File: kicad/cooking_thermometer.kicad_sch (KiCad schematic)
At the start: 41 parts, among them J1 FTDI, J2 STLINK, J3 3V3_Power, J4 Battery, J5 7SEG_CONN, J6 OLED_CONN, J7 USB_B_Micro, J8 THERMO_CONN, Q1 BC547, SW1 BOOT0_SW, SW2 NRST_SW, SW3 UI_A_SW, SW4 UI_B_SW, SW5 UI_C_SW, U1 STM32F070F6Px, U2 MCP1700x-330xxTO, U3 MCP73831-2-OT

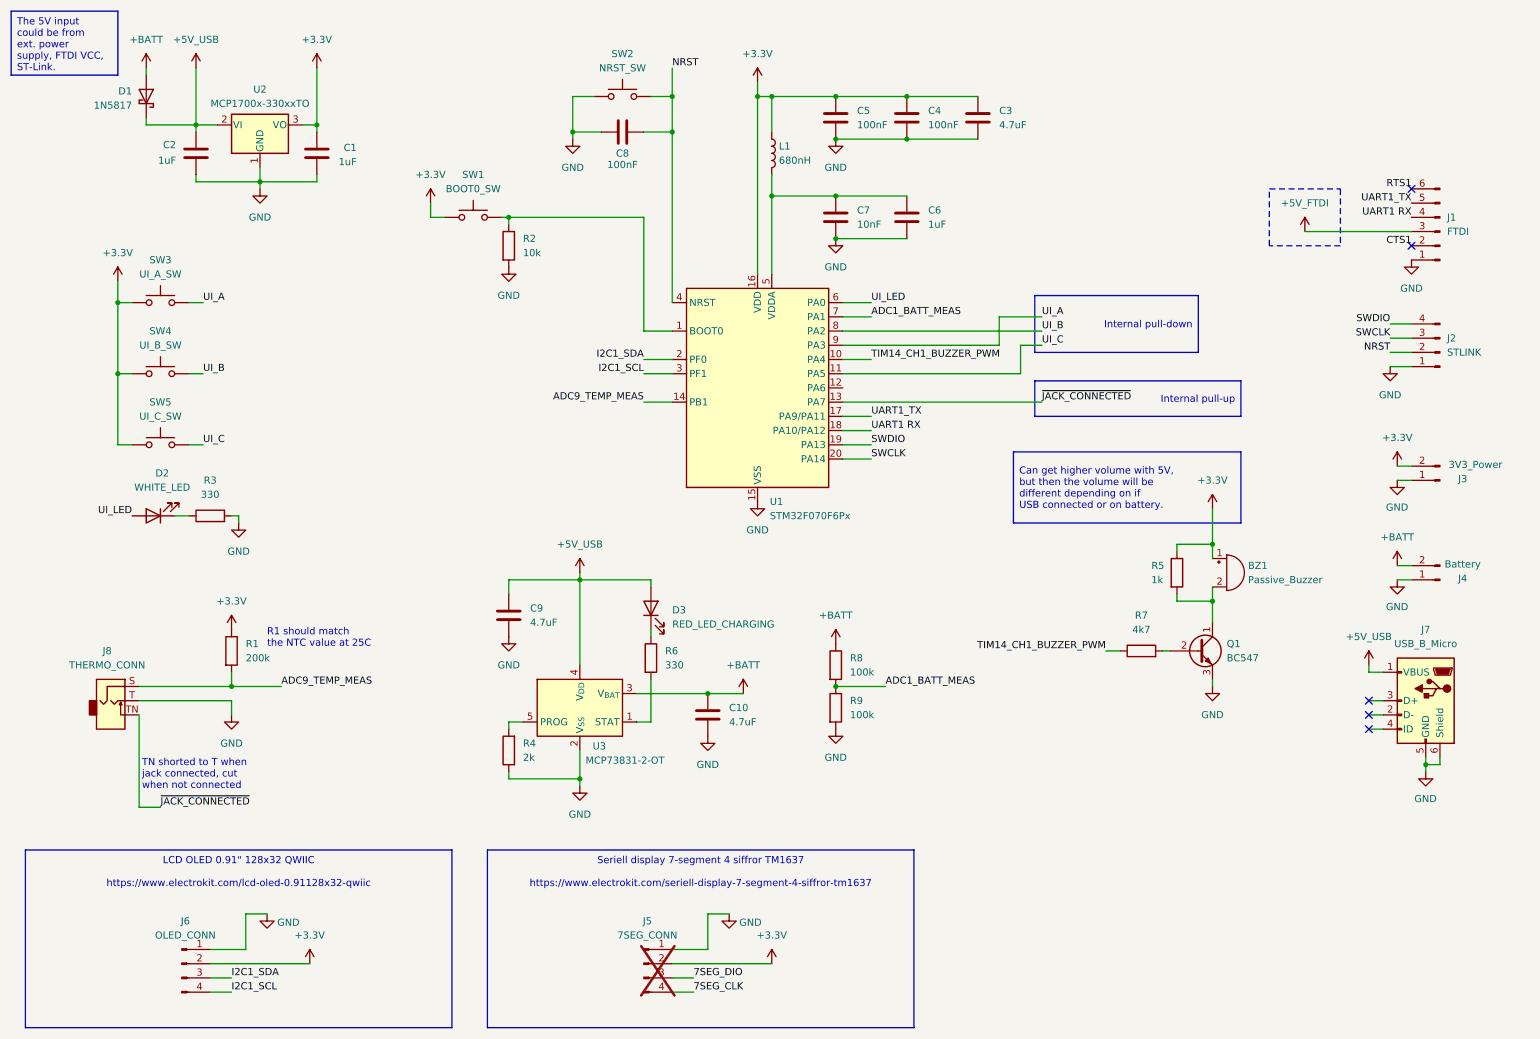
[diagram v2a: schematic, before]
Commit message: Change schematic/layout to stm32g0b0ke (LQFP32)
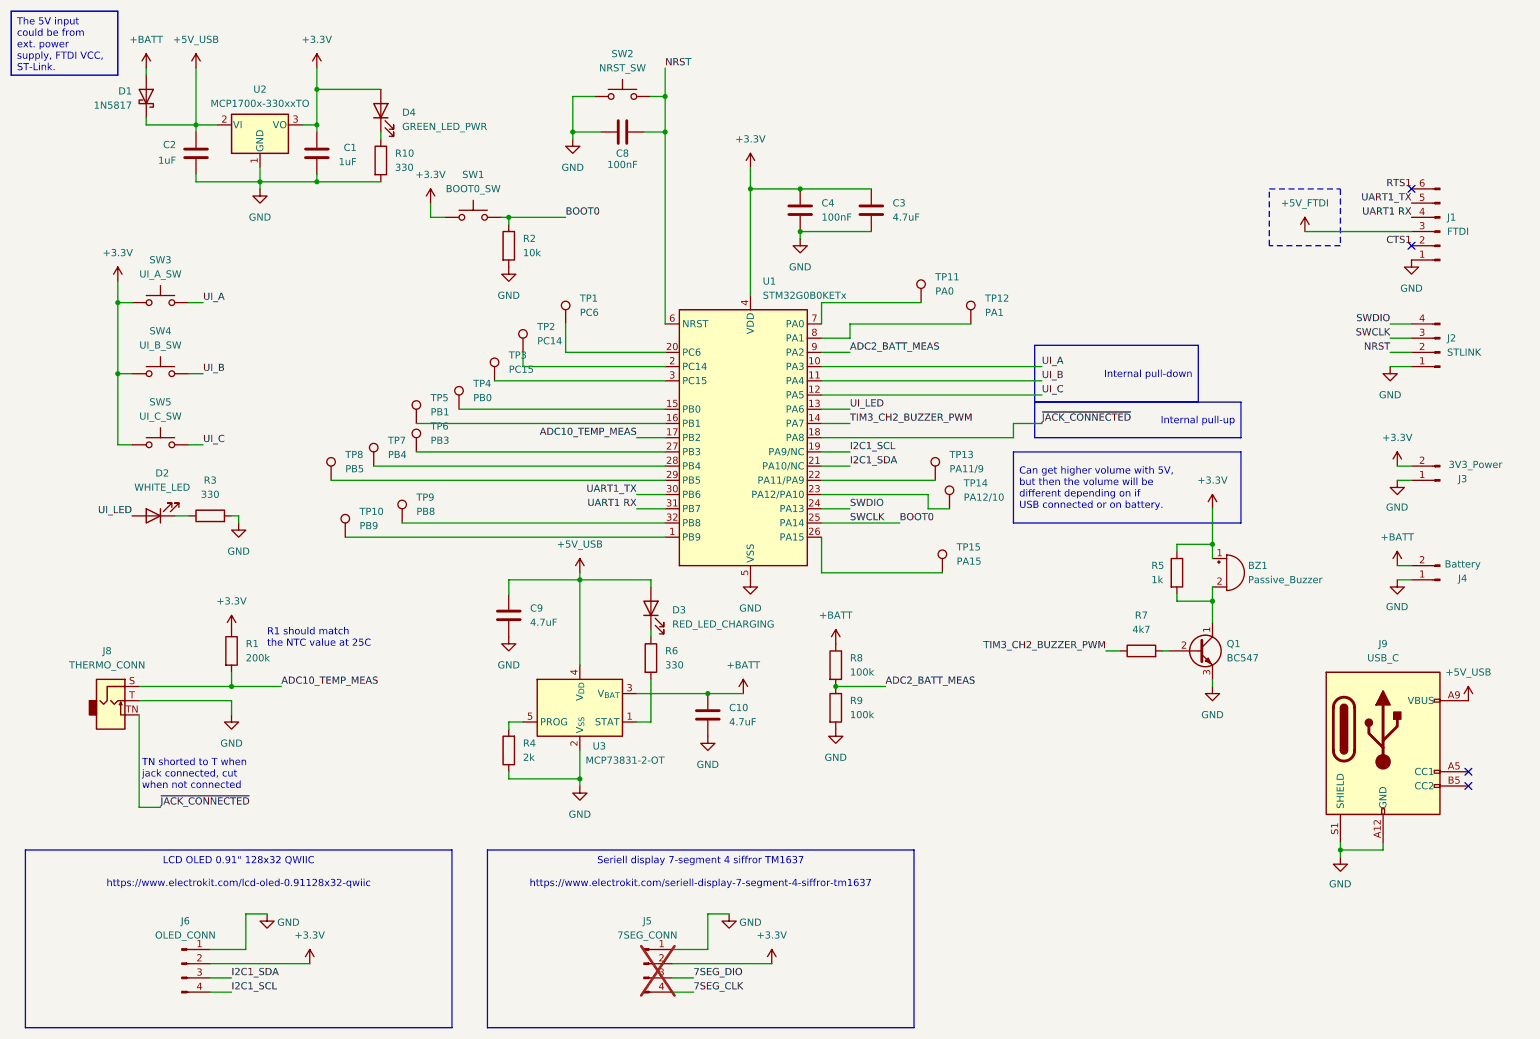
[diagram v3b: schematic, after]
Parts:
- removed C5: 100nF, Capacitor_THT:C_Disc_D3.0mm_W1.6mm_P2.50mm, symbol Device:C
- removed C6: 1uF, Capacitor_THT:C_Disc_D3.0mm_W1.6mm_P2.50mm, symbol Device:C
- removed C7: 10nF, Capacitor_THT:C_Disc_D3.0mm_W1.6mm_P2.50mm, symbol Device:C
- removed J7: USB_B_Micro, MyOwnFootprintLibrary:uUSB-B_2.54mm_connector, symbol Connector:USB_B_Micro
- removed L1: 680nH, Inductor_THT:L_Axial_L12.0mm_D5.0mm_P15.24mm_Horizontal_Fastron_MISC, symbol Device:L
- removed U1: STM32F070F6Px, MyOwnFootprintLibrary:STM32F070_DIP20, symbol MCU_ST_STM32F0:STM32F070F6Px
- added D4: GREEN_LED_PWR, LED_THT:LED_Rectangular_W5.0mm_H2.0mm, symbol Device:LED
- added J9: USB_C, Connector_USB:USB_C_Receptacle_GCT_USB4125-xx-x_6P_TopMnt_Horizontal, symbol Connector:USB_C_Receptacle_PowerOnly_6P
- added R10: 330, Resistor_SMD:R_1206_3216Metric_Pad1.30x1.75mm_HandSolder, symbol Device:R
- added TP1: PC6, TestPoint:TestPoint_Pad_D2.0mm, symbol Connector:TestPoint
- added TP10: PB9, TestPoint:TestPoint_Pad_D2.0mm, symbol Connector:TestPoint
- added TP11: PA0, TestPoint:TestPoint_Pad_D2.0mm, symbol Connector:TestPoint
- added TP12: PA1, TestPoint:TestPoint_Pad_D2.0mm, symbol Connector:TestPoint
- added TP13: PA11/9, TestPoint:TestPoint_Pad_D2.0mm, symbol Connector:TestPoint
- added TP14: PA12/10, TestPoint:TestPoint_Pad_D2.0mm, symbol Connector:TestPoint
- added TP15: PA15, TestPoint:TestPoint_Pad_D2.0mm, symbol Connector:TestPoint
- added TP2: PC14, TestPoint:TestPoint_Pad_D2.0mm, symbol Connector:TestPoint
- added TP3: PC15, TestPoint:TestPoint_Pad_D2.0mm, symbol Connector:TestPoint
- added TP4: PB0, TestPoint:TestPoint_Pad_D2.0mm, symbol Connector:TestPoint
- added TP5: PB1, TestPoint:TestPoint_Pad_D2.0mm, symbol Connector:TestPoint
- added TP6: PB3, TestPoint:TestPoint_Pad_D2.0mm, symbol Connector:TestPoint
- added TP7: PB4, TestPoint:TestPoint_Pad_D2.0mm, symbol Connector:TestPoint
- added TP8: PB5, TestPoint:TestPoint_Pad_D2.0mm, symbol Connector:TestPoint
- added TP9: PB8, TestPoint:TestPoint_Pad_D2.0mm, symbol Connector:TestPoint
- added U1: STM32G0B0KETx, Package_QFP:LQFP-32_7x7mm_P0.8mm, symbol MCU_ST_STM32G0:STM32G0B0KETx
- C1, C10, C2, C3, C4, C8, C9: footprint Capacitor_THT:C_Disc_D3.0mm_W1.6mm_P2.50mm -> Capacitor_SMD:C_1206_3216Metric_Pad1.33x1.80mm_HandSolder
- D3: footprint LED_THT:LED_D4.0mm -> LED_THT:LED_Rectangular_W5.0mm_H2.0mm
- R1, R2, R3, R4, R6, R8, R9: footprint Resistor_THT:R_Axial_DIN0207_L6.3mm_D2.5mm_P10.16mm_Horizontal -> Resistor_SMD:R_1206_3216Metric_Pad1.30x1.75mm_HandSolder
- R5, R7: footprint Resistor_THT:R_Axial_DIN0207_L6.3mm_D2.5mm_P7.62mm_Horizontal -> Resistor_SMD:R_1206_3216Metric_Pad1.30x1.75mm_HandSolder
- U2: footprint Package_TO_SOT_THT:TO-92_Inline_Wide -> Package_TO_SOT_THT:TO-92_Inline
- U3: footprint MyOwnFootprintLibrary:DIP-5-6_7.62mm_5on6 -> Package_TO_SOT_SMD:SOT-23-5_HandSoldering
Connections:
- net SWCLK is gone; now on net BOOT0: J2.3 (Pin_3)
- net +3.3V: now also D4.2 (A), U1.4 (VDD)
- net +5V_USB: now also J9.A9 (VBUS), J9.B9 (VBUS)
- net GND: now also J9.A12 (GND), J9.B12 (GND), J9.S1 (SHIELD), R10.2, U1.5 (VSS)
- net I2C1_SCL: now also U1.19 (PA9/NC)
- net I2C1_SDA: now also U1.21 (PA10/NC)
- net NRST: now also U1.6 (NRST)
- net SWDIO: now also U1.24 (PA13)
- net UART1 RX: now also U1.31 (PB7)
- net UART1_TX: now also U1.30 (PB6)
- net UI_A: now also U1.10 (PA3)
- net UI_B: now also U1.11 (PA4)
- net UI_C: now also U1.12 (PA5)
- net UI_LED: now also U1.13 (PA6)
- net ~{JACK_CONNECTED}: now also U1.18 (PA8)
- net BOOT0: now reaches R2.1, SW1.2
- net BOOT0: now also U1.25 (PA14)
- net ADC1_BATT_MEAS renamed ADC2_BATT_MEAS
- net ADC2_BATT_MEAS: now also U1.9 (PA2)
- net ADC9_TEMP_MEAS renamed ADC10_TEMP_MEAS
- net ADC10_TEMP_MEAS: now also U1.17 (PB2)
- net TIM14_CH1_BUZZER_PWM renamed TIM3_CH2_BUZZER_PWM
- net TIM3_CH2_BUZZER_PWM: now also U1.14 (PA7)
- new net: TP2.1, U1.2 (PC14)
- new net: TP5.1, U1.16 (PB1)
- new net: TP9.1, U1.32 (PB8)
- new net: TP3.1, U1.3 (PC15)
- new net: D4.1 (K), R10.1
- new net: TP1.1, U1.20 (PC6)
- new net: TP6.1, U1.27 (PB3)
- new net: TP7.1, U1.28 (PB4)
- new net: TP13.1, U1.22 (PA11/PA9)
- new net: TP8.1, U1.29 (PB5)
- new net: TP4.1, U1.15 (PB0)
- new net: TP15.1, U1.26 (PA15)
- new net: TP14.1, U1.23 (PA12/PA10)
- new net: TP10.1, U1.1 (PB9)
- new net: TP11.1, U1.7 (PA0)
- new net: TP12.1, U1.8 (PA1)
- no-connect marks 5 -> 4
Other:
- moved on the sheet: C3, C4

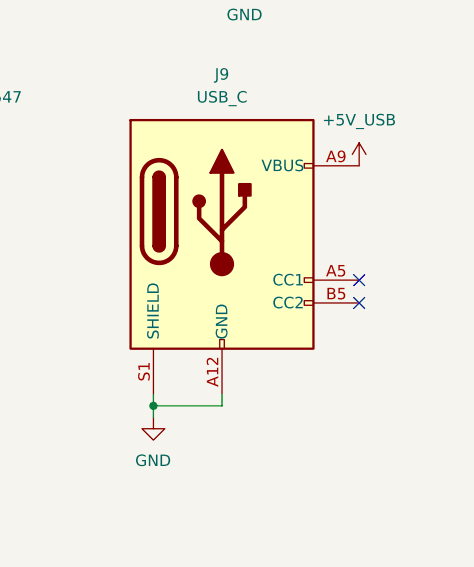
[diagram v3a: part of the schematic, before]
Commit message: Change to longer pads and some other adjustments
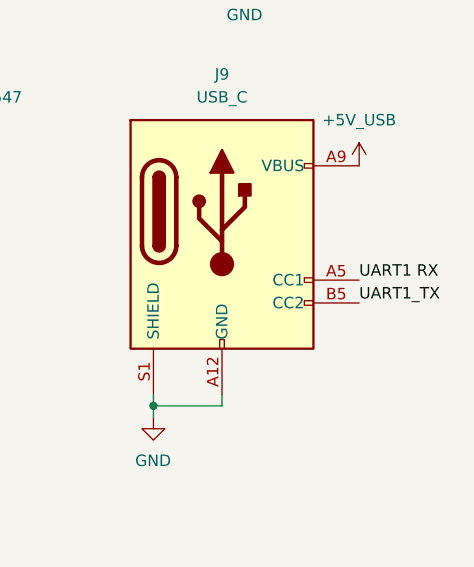
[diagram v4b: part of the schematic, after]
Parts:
- J9: footprint Connector_USB:USB_C_Receptacle_GCT_USB4125-xx-x_6P_TopMnt_Horizontal -> MyOwnFootprintLibrary:USB_C_Receptacle_GCT_USB4125-xx-x_6P_TopMnt_Horizontal_Long_Pads
- U1: footprint Package_QFP:LQFP-32_7x7mm_P0.8mm -> MyOwnFootprintLibrary:LQFP-32_7x7mm_P0.8mm_Long_pads
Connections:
- net UART1 RX: now also J9.A5 (CC1)
- net UART1_TX: now also J9.B5 (CC2)
- no-connect marks 4 -> 2
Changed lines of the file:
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@@
 	)
 	(no_connect
-		(at 274.32 152.4)
-	)
-	(no_connect
 		(at 264.16 55.88)
 	)
 	(no_connect
-		(at 274.32 149.86)
-	)
-	(no_connect
 		(at 264.16 45.72)
 	)
@@
 		)
 	)
+	(label "UART1_TX"
+		(at 274.32 152.4 0)
+		(fields_autoplaced yes)
+		(effects
+			(font
+				(size 1.27 1.27)
+			)
+			(justify left bottom)
+		)
+	)
 	(label "TIM3_CH2_BUZZER_PWM"
 		(at 163.83 87.63 0)
@@
 		)
 	)
+	(label "UART1 RX"
+		(at 274.32 149.86 0)
+		(fields_autoplaced yes)
+		(effects
+			(font
+				(size 1.27 1.27)
+			)
+			(justify left bottom)
+		)
+	)
 	(label "BOOT0"
 		(at 172.72 105.41 0)
@@
 			)
 		)
-		(property "Footprint" "Connector_USB:USB_C_Receptacle_GCT_USB4125-xx-x_6P_TopMnt_Horizontal"
+		(property "Footprint" "MyOwnFootprintLibrary:USB_C_Receptacle_GCT_USB4125-xx-x_6P_TopMnt_Horizontal_Long_Pads"
 			(at 262.89 142.24 0)
 			(effects
@@
 			)
 		)
-		(property "Footprint" "Package_QFP:LQFP-32_7x7mm_P0.8mm"
+		(property "Footprint" "MyOwnFootprintLibrary:LQFP-32_7x7mm_P0.8mm_Long_pads"
 			(at 133.35 113.03 0)
 			(effects

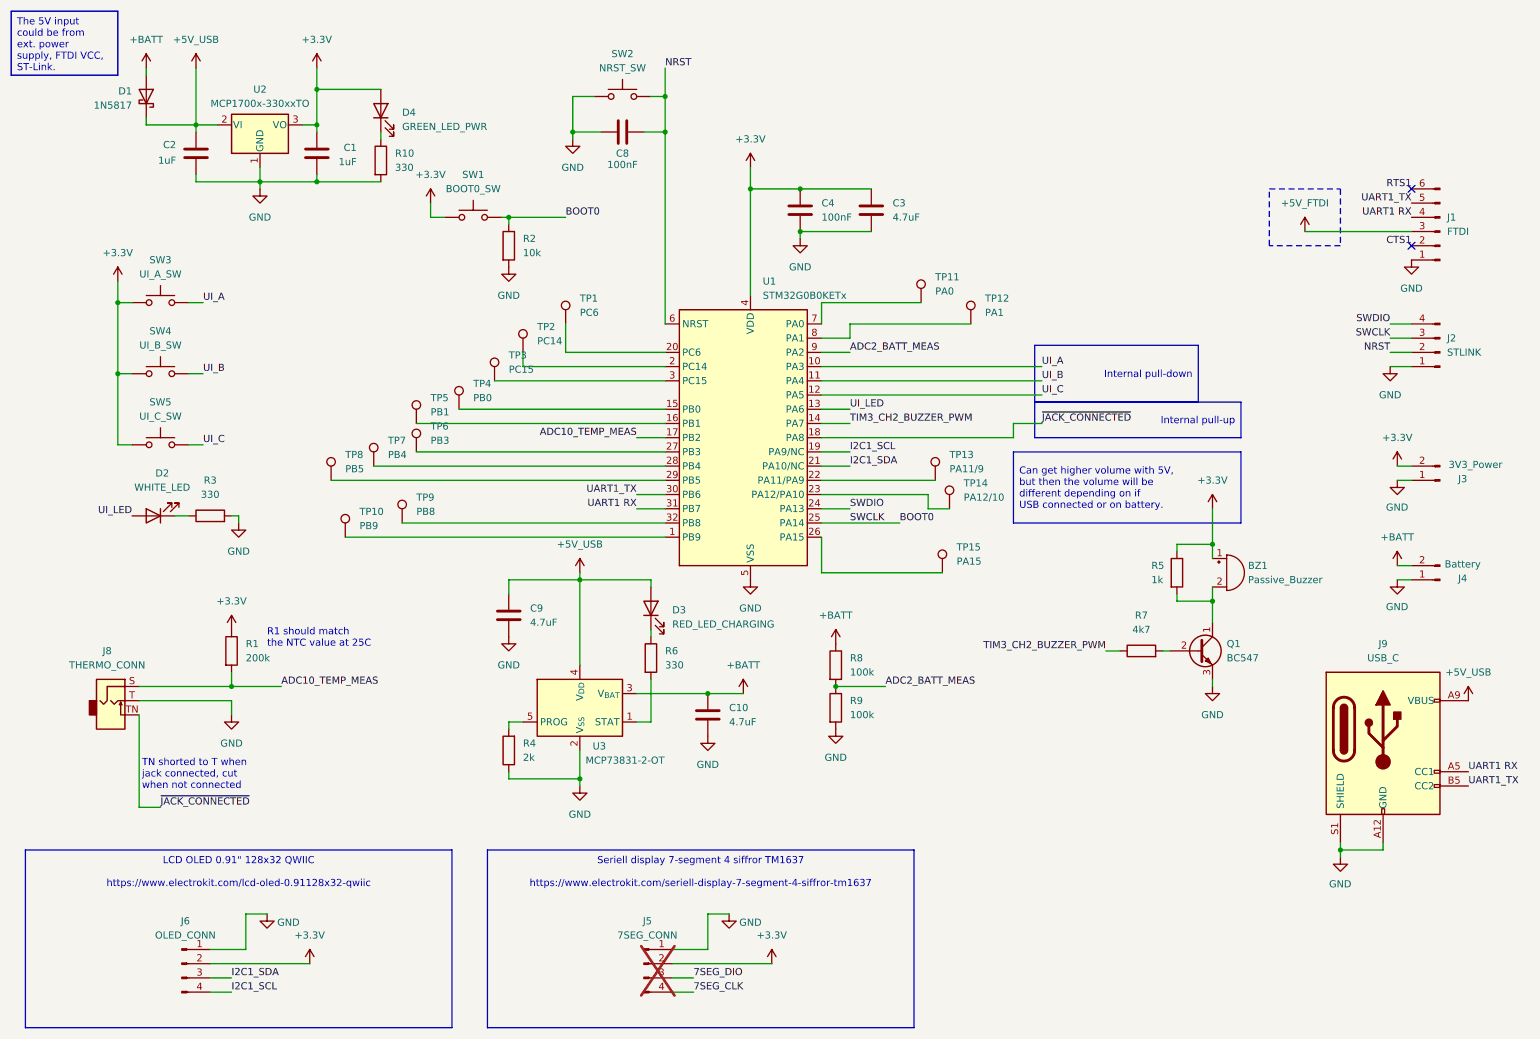
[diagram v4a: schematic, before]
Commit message: Change 2.5mm jack, make the board bigger, add mounting holes. Some rewiring.
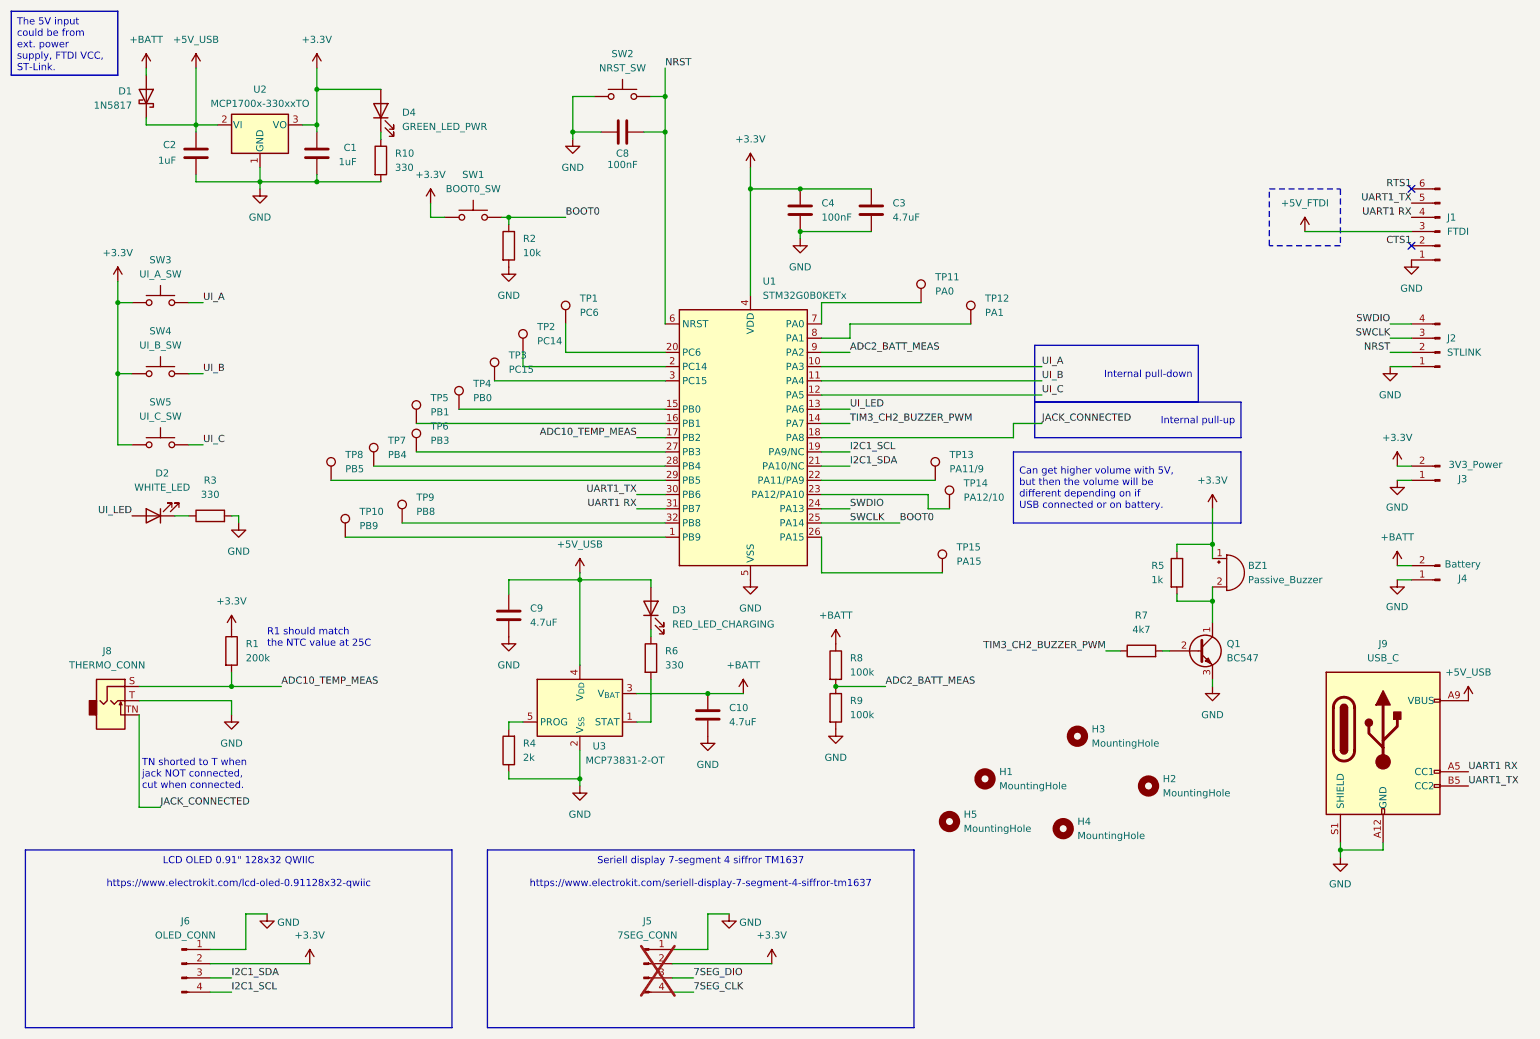
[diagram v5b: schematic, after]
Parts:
- added H1, H2, H3, H4, H5: MountingHole, MountingHole:MountingHole_3.2mm_M3, symbol Mechanical:MountingHole
- J8: footprint MyOwnFootprintLibrary:AudioJack_Mono_2.5mm_with_Tip-Detect -> MyOwnFootprintLibrary:Jack_Mono_2.5mm_with_Tip-Detect_Electrokit_41010270
- J9: footprint MyOwnFootprintLibrary:USB_C_Receptacle_GCT_USB4125-xx-x_6P_TopMnt_Horizontal_Long_Pads -> MyOwnFootprintLibrary:USB_C_Receptacle_6P_TopMnt_Horizontal_Long_Pads_Electrokit_41021035
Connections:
- net ~{JACK_CONNECTED} renamed JACK_CONNECTED
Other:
- note added: "TN shorted to T when jack NOT connected, cut when connected."
- note removed: "TN shorted to T when jack connected, cut when not connected"
